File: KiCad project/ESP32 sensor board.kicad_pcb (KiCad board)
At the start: 4 copper layers, 104.8 x 50 mm, 82 parts, among them J1 USB_C_Receptacle, J2 JST_2mm_LiPo, J3 GSD090012SEU, J4 B4B-XH-AM, J6 Conn_01x05, Q1 TEMT6000X01, Q2 BC817, Q3 BC817, SW1 1101NE, SW2 1101NE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

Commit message: Completed draft of the layout.
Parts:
- added G***: LOGO, Footprints:TE_Logo_11.6x4, B.Cu at (189.7, 107.3)
- added REF**: OSHW-Logo_5.7x6mm_SilkScreen, Symbol:OSHW-Logo_5.7x6mm_SilkScreen, B.Cu at (189.7, 99.2)
- added REF**: KiCad-Logo2_5mm_SilkScreen, Symbol:KiCad-Logo2_5mm_SilkScreen, B.Cu at (190.0, 91.2)
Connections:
- net Net-(D4-K) renamed /PWR_LED
- net Net-(U1-STAT1/~{LBO}) renamed /CHARGED
- net Net-(U1-STAT2) renamed /CHARGING
- net Net-(U1-~{PG}) renamed /CHARGING_POWER_GOOD
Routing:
- net Net-(C19-Pad2): track 8.14 -> 6.96 mm
- net Net-(J3-CLK): track 7.49 -> 6.51 mm
- net /+5V_USB: track 75.9 -> 75.0 mm
- net /ESP32-C3-02/MIC_OUT: track 48.2 -> 49.0 mm
- net 3.3V: track 69.8 -> 69.1 mm
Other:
- board text added: "3V3"
- board text added: "BOOT"
- board text added: "CHARGE POWER GOOD"
- board text added: "CHARGED"
- board text added: "CHARGING"
- board text added: "EN"
- board text added: "GND"
- board text added: "IO18"
- board text added: "IO19"
- board text added: "IO8"
- board text added: "PWR"
- board text added: "RX"
- board text added: "SCL"
- board text added: "SDA"
- board text added: "TX"

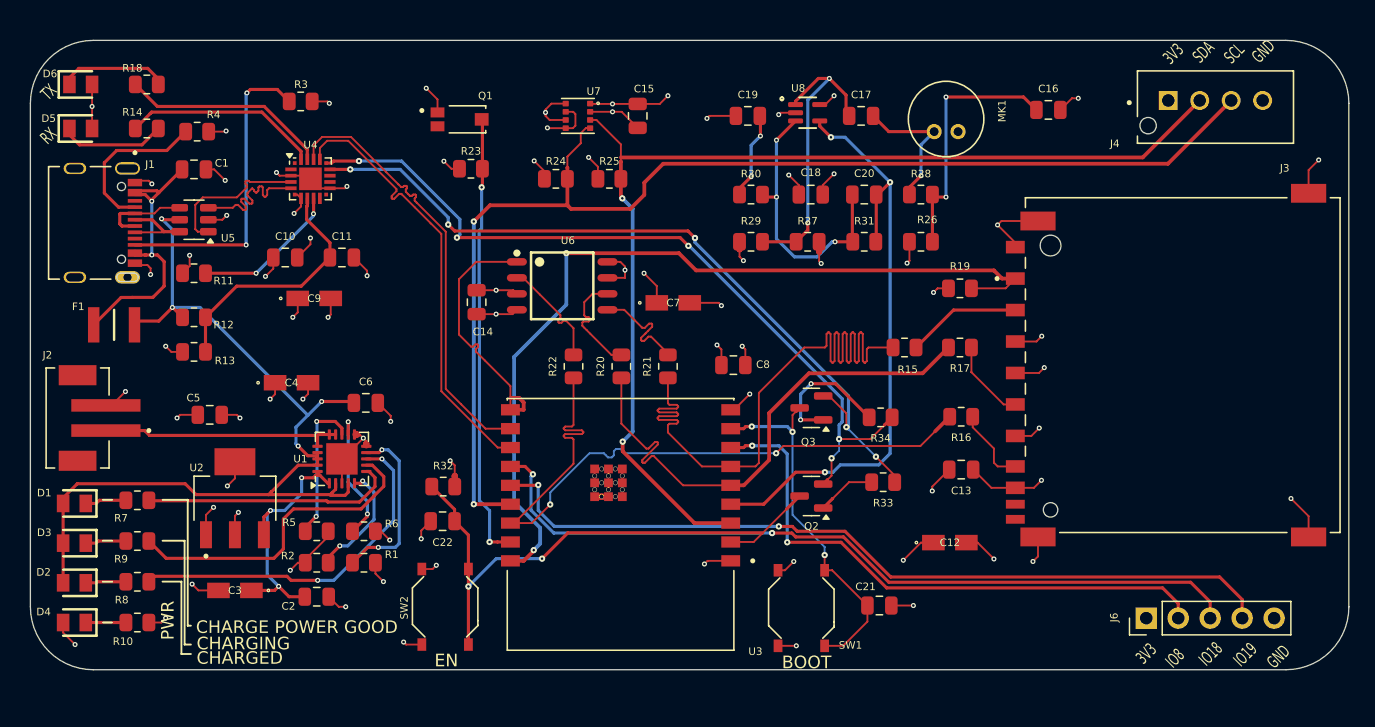
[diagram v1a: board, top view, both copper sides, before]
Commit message: Replaced USB C receptacle with a different model. Repositioning components to better align with manufacturer recommendations.
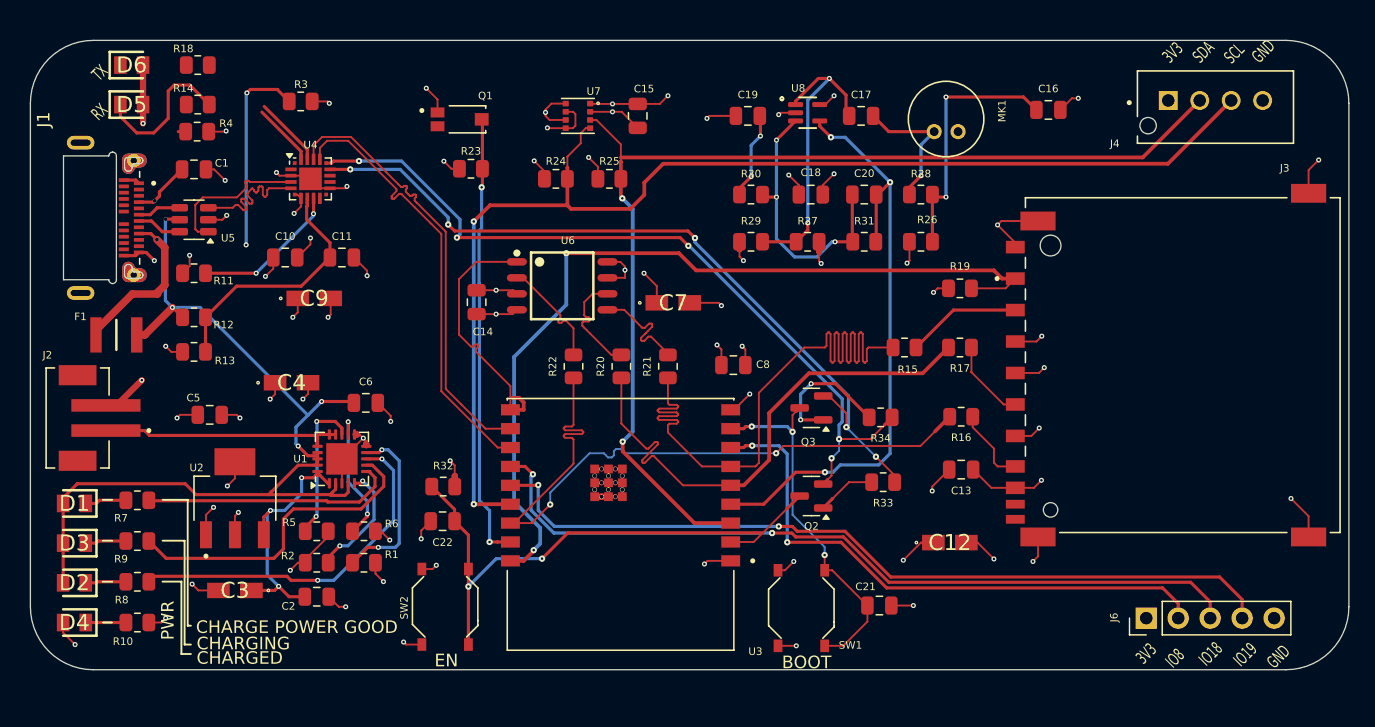
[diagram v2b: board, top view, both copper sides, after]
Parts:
- removed G***: LOGO, Footprints:TE_Logo_11.6x4
- removed REF**: OSHW-Logo_5.7x6mm_SilkScreen, Symbol:OSHW-Logo_5.7x6mm_SilkScreen
- removed REF**: KiCad-Logo2_5mm_SilkScreen, Symbol:KiCad-Logo2_5mm_SilkScreen
- J1: footprint Footprints:VALCON_CSP-USC16-TR -> Footprints:TE_1-2295018-2
- moved D5 4.47 mm to (106.3, 77.6)
- moved R14 4.47 mm to (111.5, 77.6)
- moved J1 4.33 mm to (102.2, 86.6)
- moved D6 4.33 mm to (106.3, 74.5)
- moved R18 4.33 mm to (111.5, 74.5)
- moved F1 0.82 mm to (105.1, 95.9)
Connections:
- U5 pad 4: /USB_DN -> /USB_DP
- U5 pad 6: /USB_DP -> /USB_DN
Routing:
- net Net-(J1-CC1): track 12.8 -> 0.59 mm
- net Net-(U4-~{RXT}/GPIO.3): track 16.6 -> 5.62 mm
- net Net-(U4-~{TXT}/GPIO.2): track 15.6 -> 5.04 mm
- net Net-(J1-CC2): track 24.8 -> 16.0 mm
- net Net-(D6-K): track 8.68 -> 0.96 mm
- net /USB_DP: track 7.69 -> 3.47 mm
- net Net-(D5-K): track 8.43 -> 12.0 mm
- net /USB_DN: track 7.02 -> 3.59 mm
- net GND: track 128.9 -> 131.7 mm, vias 51 -> 50
- net 3.3V: track 69.1 -> 70.2 mm

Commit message: Work in progress, new layout and routing.
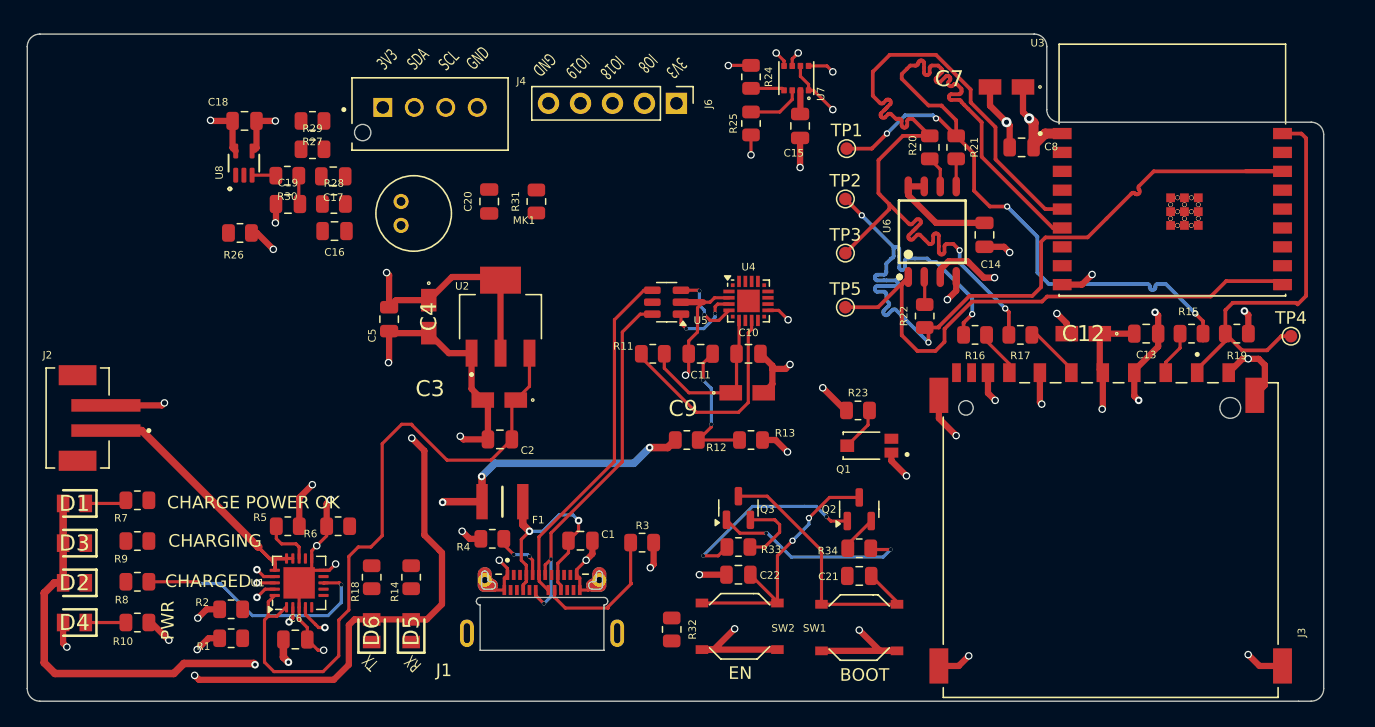
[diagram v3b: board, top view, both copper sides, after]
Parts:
- added TP1: Test MOSI, TestPoint:TestPoint_Pad_D1.0mm, F.Cu at (163.1, 81.1)
- added TP2: Test MISO, TestPoint:TestPoint_Pad_D1.0mm, F.Cu at (163.0, 85.1)
- added TP3: Test CLK, TestPoint:TestPoint_Pad_D1.0mm, F.Cu at (163.0, 89.4)
- added TP4: TEST CS_SD, TestPoint:TestPoint_Pad_D1.0mm, F.Cu at (198.4, 96.0)
- added TP5: TEST CS, TestPoint:TestPoint_Pad_D1.0mm, F.Cu at (163.0, 93.7)
- moved J4 62.4 mm to (130.0, 78.3)
- moved C16 57.5 mm to (122.4, 87.7), turned to 180 degrees
- moved J6 55.4 mm to (149.6, 77.5), turned to -90 degrees
- moved R26 54.1 mm to (114.9, 87.8), turned to 0 degrees
- moved U3 52.1 mm to (189.0, 82.8), turned to 0 degrees
- moved J1 49.3 mm to (138.9, 119.6), turned to 0 degrees
- moved D6 48.8 mm to (125.4, 119.4), turned to 90 degrees
- moved D5 47.3 mm to (128.5, 119.4), turned to 90 degrees
- moved R28 46.6 mm to (122.4, 85.5)
- moved C18 45.4 mm to (115.3, 78.9), turned to 0 degrees
- moved U8 45.0 mm to (115.2, 82.2), turned to 90 degrees
- moved R13 44.8 mm to (155.5, 104.2), turned to 0 degrees
- moved R3 44.3 mm to (146.8, 112.4)
- moved R18 43.0 mm to (125.4, 115.2), turned to 90 degrees
- moved MK1 43.0 mm to (128.7, 86.2), turned to 180 degrees
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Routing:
- net /ESP32-C3-02/SCL: track 98.3 -> 2.69 mm, vias 2 -> 0
- net /ESP32-C3-02/SDA: track 88.5 -> 4.41 mm, vias 2 -> 0
- net /ESP32-C3-02/GPIO18: track 64.6 -> 0.00 mm, vias 2 -> 0
- net /ESP32-C3-02/GPIO19: track 64.6 -> 0.00 mm, vias 2 -> 0
- net /ESP32-C3-02/RTS: track 63.7 -> 2.93 mm, vias 5 -> 0
- net /ESP32-C3-02/DTS: track 61.6 -> 5.93 mm, vias 5 -> 0
- net 3.3V: track 70.2 -> 124.1 mm, vias 29 -> 15
- net /ESP32-C3-02/MIC_OUT: track 49.0 -> 0.00 mm, vias 3 -> 0
- net /ESP32-C3-02/GPIO8: track 47.4 -> 0.00 mm, vias 2 -> 0
- net /ESP32-C3-02/RX_TX: track 35.0 -> 0.00 mm
- net /ESP32-C3-02/CS_SD: track 68.9 -> 34.0 mm, vias 2 -> 0
- net GND: track 131.7 -> 166.5 mm, vias 50 -> 41
- net /ESP32-C3-02/TX_RX: track 34.9 -> 0.00 mm
- net +5V: track 20.6 -> 53.2 mm, vias 3 -> 0
- net /ESP32-C3-02/PHOTO_C: track 35.7 -> 3.54 mm, vias 2 -> 0
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- added copper zone on In1.Cu, net /+5V_USB
- added copper zone on In1.Cu, net 3.3V
- removed copper zone on In1.Cu, net GND
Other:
- board size 104.8 x 50 mm -> 103 x 53 mm
- board text added: "CHARGE POWER OK"
- board text removed: "CHARGE POWER GOOD"

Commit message: Moving thigns around.
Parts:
- moved D1 29.7 mm to (115.6, 83.0)
- moved R7 29.7 mm to (120.6, 82.7)
- moved D2 29.7 mm to (115.6, 89.3)
- moved D3 29.7 mm to (115.6, 86.1)
- moved D4 29.7 mm to (115.6, 92.5)
- moved R10 29.7 mm to (120.6, 92.5)
- moved R8 29.7 mm to (120.6, 89.2)
- moved R9 29.7 mm to (120.6, 86.0)
- moved C18 29.3 mm to (144.5, 80.8)
- moved R28 29.3 mm to (151.6, 87.5)
- moved C16 29.3 mm to (151.6, 89.6)
- moved C17 29.3 mm to (151.5, 85.2)
- moved C19 29.3 mm to (147.9, 87.5)
- moved R26 29.3 mm to (144.1, 89.8)
- moved R27 29.3 mm to (149.9, 80.8)
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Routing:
- net /+5V_USB: track 63.5 -> 39.4 mm, vias 10 -> 9
- net /CHARGED: track 19.7 -> 0.07 mm, vias 2 -> 0
- net /VBAT: track 23.3 -> 7.40 mm
- net 3.3V: track 124.1 -> 111.1 mm, vias 15 -> 13
- net GND: track 166.5 -> 156.1 mm, vias 41 -> 37
- removed copper zone on In1.Cu, net /+5V_USB

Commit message: Completed layout for v2.
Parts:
- added G***: LOGO, Footprints:TE_Logo_11.6x4, F.Cu at (163.0, 102.8)
- J1: footprint Footprints:TE_1-2295018-2 -> Footprints:BELFUSE_SS-52400-002
- moved R7 30.5 mm to (116.5, 112.9), turned to 90 degrees
- moved D6 28.9 mm to (143.5, 96.9)
- moved J6 28.0 mm to (114.9, 88.6), turned to 0 degrees
- moved R9 27.0 mm to (119.5, 113.0), turned to 90 degrees
- moved D1 25.8 mm to (116.5, 108.8), turned to 90 degrees
- moved D5 25.5 mm to (140.4, 96.9)
- moved R8 24.8 mm to (113.5, 113.0), turned to 90 degrees
- moved D3 23.0 mm to (119.6, 108.8), turned to 90 degrees
- moved R18 22.9 mm to (143.5, 101.2)
- moved Q1 22.0 mm to (151.5, 87.2)
- moved R23 22.0 mm to (150.6, 84.5)
- moved D2 19.6 mm to (113.4, 108.8), turned to 90 degrees
- moved R14 18.4 mm to (140.4, 101.2)
- moved MK1 17.5 mm to (147.0, 78.8), turned to 0 degrees
- moved U5 17.3 mm to (146.2, 110.4), turned to -90 degrees
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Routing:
- net GND: track 156.1 -> 473.5 mm, vias 37 -> 43
- net /ESP32-C3-02/GPIO19: track 0.00 -> 130.3 mm, vias 0 -> 1
- net /ESP32-C3-02/GPIO18: track 0.00 -> 104.2 mm, vias 0 -> 2
- net /ESP32-C3-02/SCL: track 2.69 -> 101.0 mm, vias 0 -> 4
- net /ESP32-C3-02/GPIO8: track 0.00 -> 78.9 mm, vias 0 -> 4
- net /ESP32-C3-02/SDA: track 4.41 -> 83.2 mm, vias 0 -> 3
- net /ESP32-C3-02/MIC_OUT: track 0.00 -> 68.7 mm
- net /ESP32-C3-02/RX_TX: track 0.00 -> 68.4 mm, vias 0 -> 2
- net /ESP32-C3-02/TX_RX: track 0.00 -> 64.6 mm, vias 0 -> 2
- net /ESP32-C3-02/PHOTO_C: track 3.54 -> 63.4 mm, vias 0 -> 2
- net /ESP32-C3-02/EN: track 21.6 -> 71.7 mm, vias 2 -> 4
- net /ESP32-C3-02/BOOT: track 21.8 -> 68.8 mm, vias 0 -> 2
- net /ESP32-C3-02/SCLK: track 69.0 -> 43.6 mm
- net /ESP32-C3-02/MOSI_DI: track 75.4 -> 51.1 mm
- net /ESP32-C3-02/RTS: track 2.93 -> 26.8 mm, vias 0 -> 2
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- added copper zone on In2.Cu, net /+5V_USB
- added copper zone on F.Cu, net 3.3V
- added copper zone on In2.Cu, net GND
- removed copper zone on In2.Cu, net 3.3V
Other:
- board size 103 x 53 mm -> 89.5 x 52.8 mm
- board text added: "CHARGE PWR OK"
- board text added: "CS"
- board text added: "CS_SD"
- board text added: "Charger"
- board text added: "ESP32 S3"
- board text added: "Environment sensor"
- board text added: "Flash memory"
- board text added: "Light sensor"
- board text added: "MISO"
- board text added: "MOSI"
- board text added: "RESET & BOOT"
- board text added: "Regulator"
- board text added: "SLCK"
- board text added: "Sound sensor"
- board text added: "USB"
- board text removed: "CHARGE POWER OK"

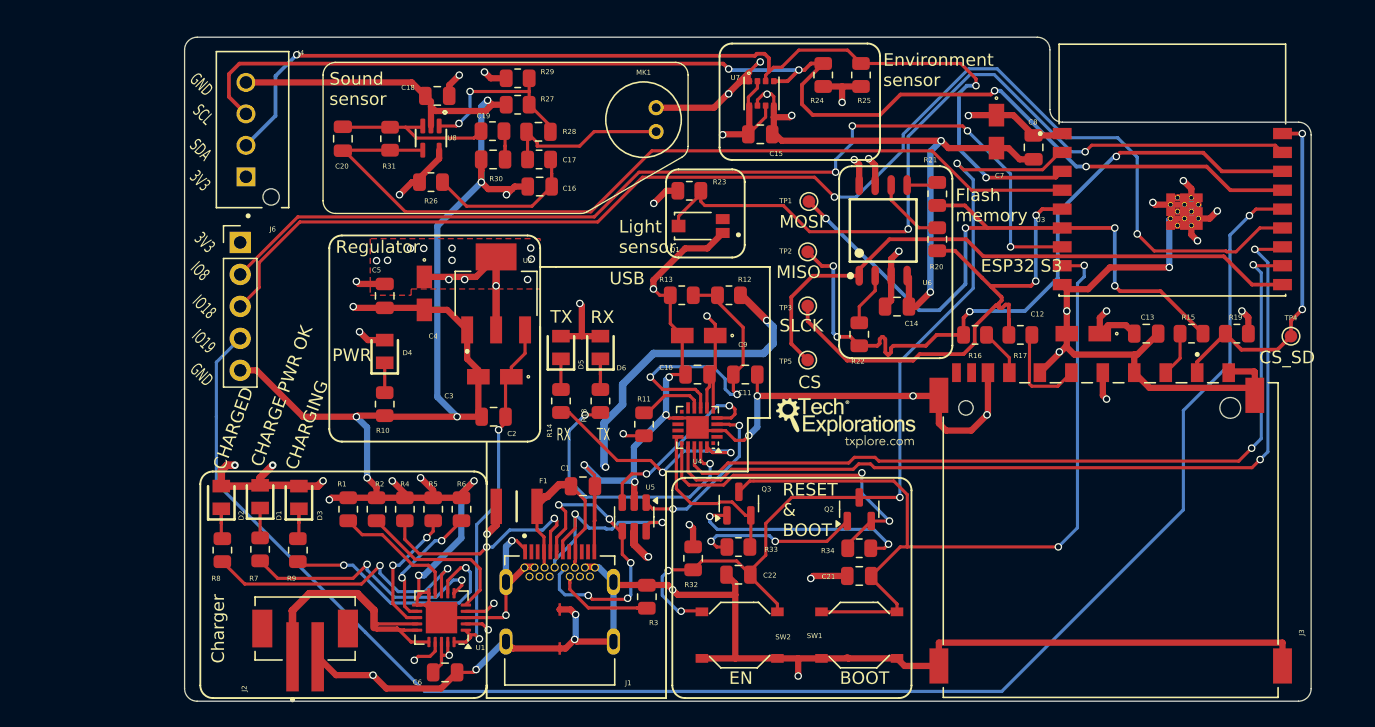
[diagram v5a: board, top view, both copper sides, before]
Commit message: Introduced new parts that can be purchased for manufacturing by NextPCB. Corrected numerous issues.
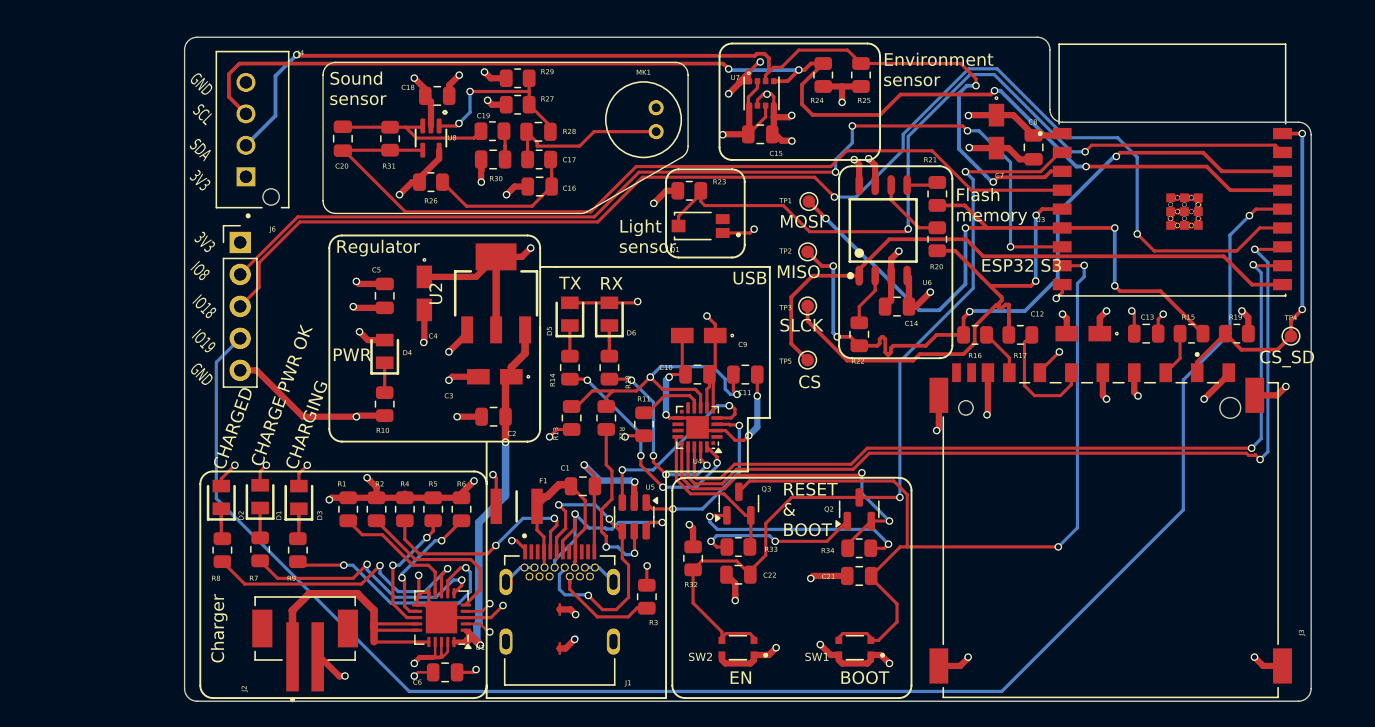
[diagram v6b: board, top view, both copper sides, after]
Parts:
- removed G***: LOGO, Footprints:TE_Logo_11.6x4
- SW1, SW2: footprint Footprints:SW4-SMD-5.2X5.2X1.5MM -> Footprints:SW_USLPT2819DT2TR
- U2: footprint Footprints:VREG_LM1117MPX-3.3_NOPB -> Footprints:VREG_LM1117MPX-3.3
- moved R12 13.8 mm to (144.0, 102.5), turned to 90 degrees
- moved R13 13.1 mm to (141.2, 102.5), turned to -90 degrees
- moved D5 2.74 mm to (141.1, 94.2)
- moved D6 2.74 mm to (144.2, 94.2)
- moved R14 2.74 mm to (141.1, 98.5)
- moved R18 2.74 mm to (144.2, 98.5)
- moved SW1 1.06 mm to (163.8, 120.8)
- moved SW2 1.01 mm to (154.5, 120.8)
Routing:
- net GND: track 473.5 -> 200.5 mm, vias 43 -> 52
- net /+5V_USB: track 56.0 -> 35.6 mm, vias 11 -> 10
- net Net-(U4-~{RXT}/GPIO.3): track 22.4 -> 16.0 mm, vias 2 -> 4
- net /ESP32-C3-02/EN: track 71.7 -> 68.2 mm, vias 4 -> 2
- net Net-(J3-CLK): track 7.82 -> 9.64 mm
- net 3.3V: track 89.4 -> 90.5 mm, vias 31 -> 21
- net Net-(U4-~{TXT}/GPIO.2): track 18.3 -> 19.3 mm, vias 2 -> 4
- net +5V: track 29.6 -> 30.4 mm
- net /ESP32-C3-02/BOOT: track 68.8 -> 69.6 mm
- net /ESP32-C3-02/USB_D+: track 13.6 -> 14.3 mm
- net /ESP32-C3-02/GPIO19: track 130.3 -> 131.0 mm
- net /ESP32-C3-02/RX_TX: track 68.4 -> 69.1 mm
- net /ESP32-C3-02/USB_D-: track 15.1 -> 15.7 mm
- net /ESP32-C3-02/TX_RX: track 64.6 -> 65.2 mm
- net Net-(J1-CC2): track 8.28 -> 8.86 mm
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- added copper zone on In2.Cu, net 3.3V
- added copper zone on In1.Cu, net GND
- removed copper zone on F.Cu, net 3.3V
- removed copper zone on In1.Cu, net 3.3V
- removed copper zone on In2.Cu, net GND

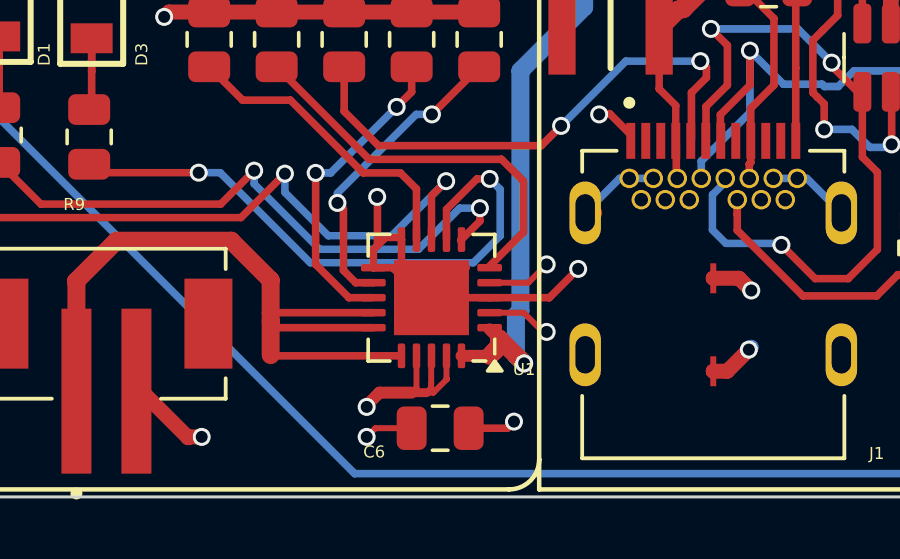
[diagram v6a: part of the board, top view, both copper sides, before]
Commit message: Updated U1 footprint to better match the component we can order from Microchip.
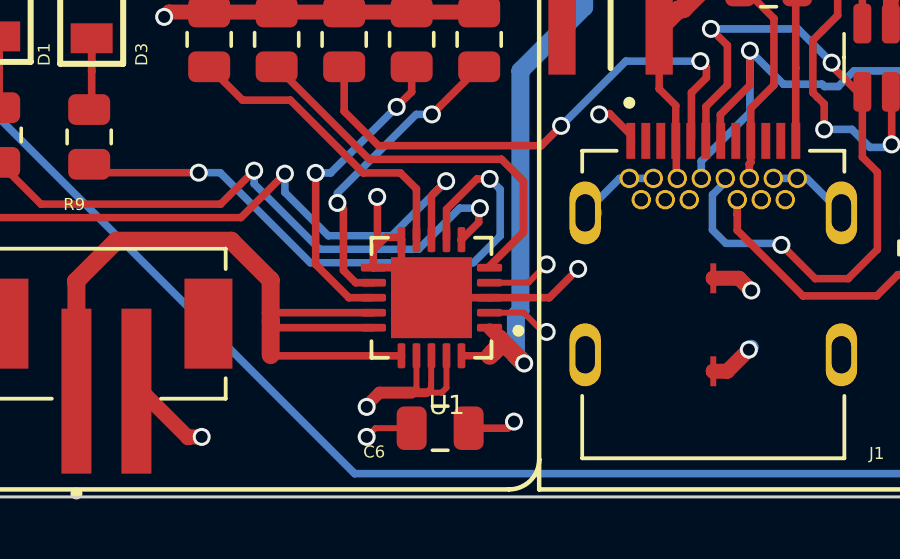
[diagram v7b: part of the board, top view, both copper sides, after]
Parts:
- U1: footprint Package_DFN_QFN:QFN-20-1EP_4x4mm_P0.5mm_EP2.5x2.5mm -> Footprints:QFN50P400X400X100-21N
